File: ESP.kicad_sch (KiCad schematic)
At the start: 15 parts, among them J1 Conn_01x20_Pin, J2 Conn_01x20_Pin, J3 Conn_01x04_Pin, SW1 SW_Push, SW2 SW_Push, U3 AMS1117-3.3, U4 ESP32-S3-WROOM-1

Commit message: chore: add README (#2)
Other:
- title: (none) -> ESP32 PoE
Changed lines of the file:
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@@
 	(generator_version "9.0")
 	(paper "A4")
+	(title_block
+		(title "ESP32 PoE")
+		(rev "v0.1.0")
+	)
 	(rectangle
 		(start 16.51 161.29)

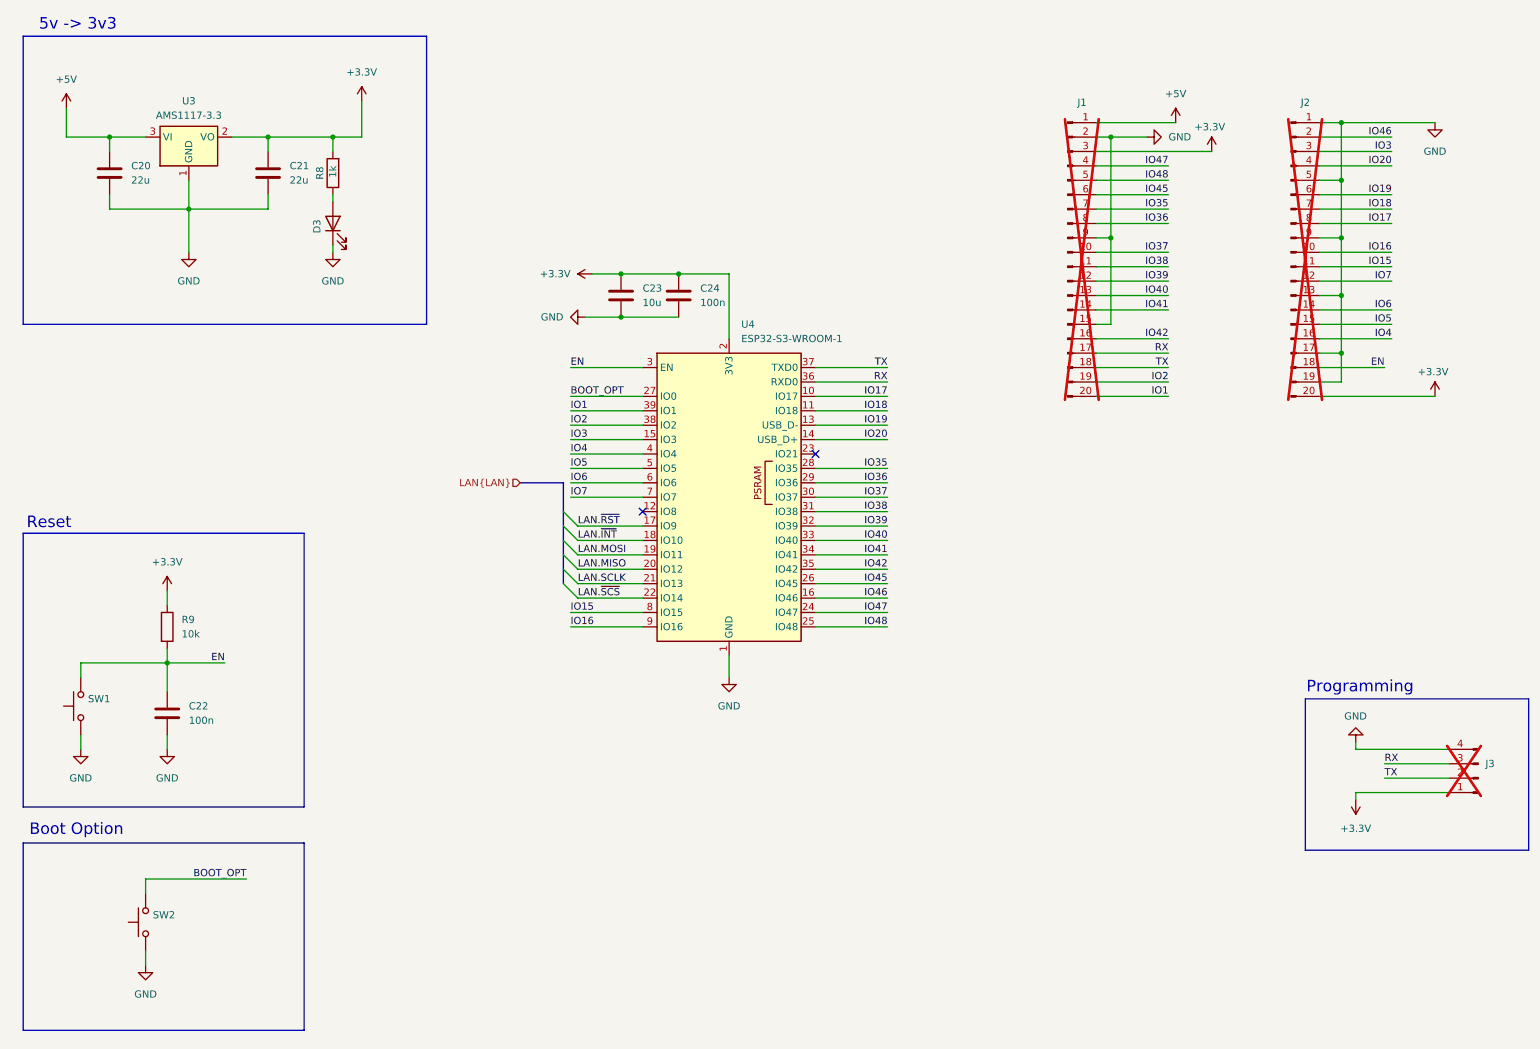
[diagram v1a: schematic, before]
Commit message: feat: redesign to smaller form factor
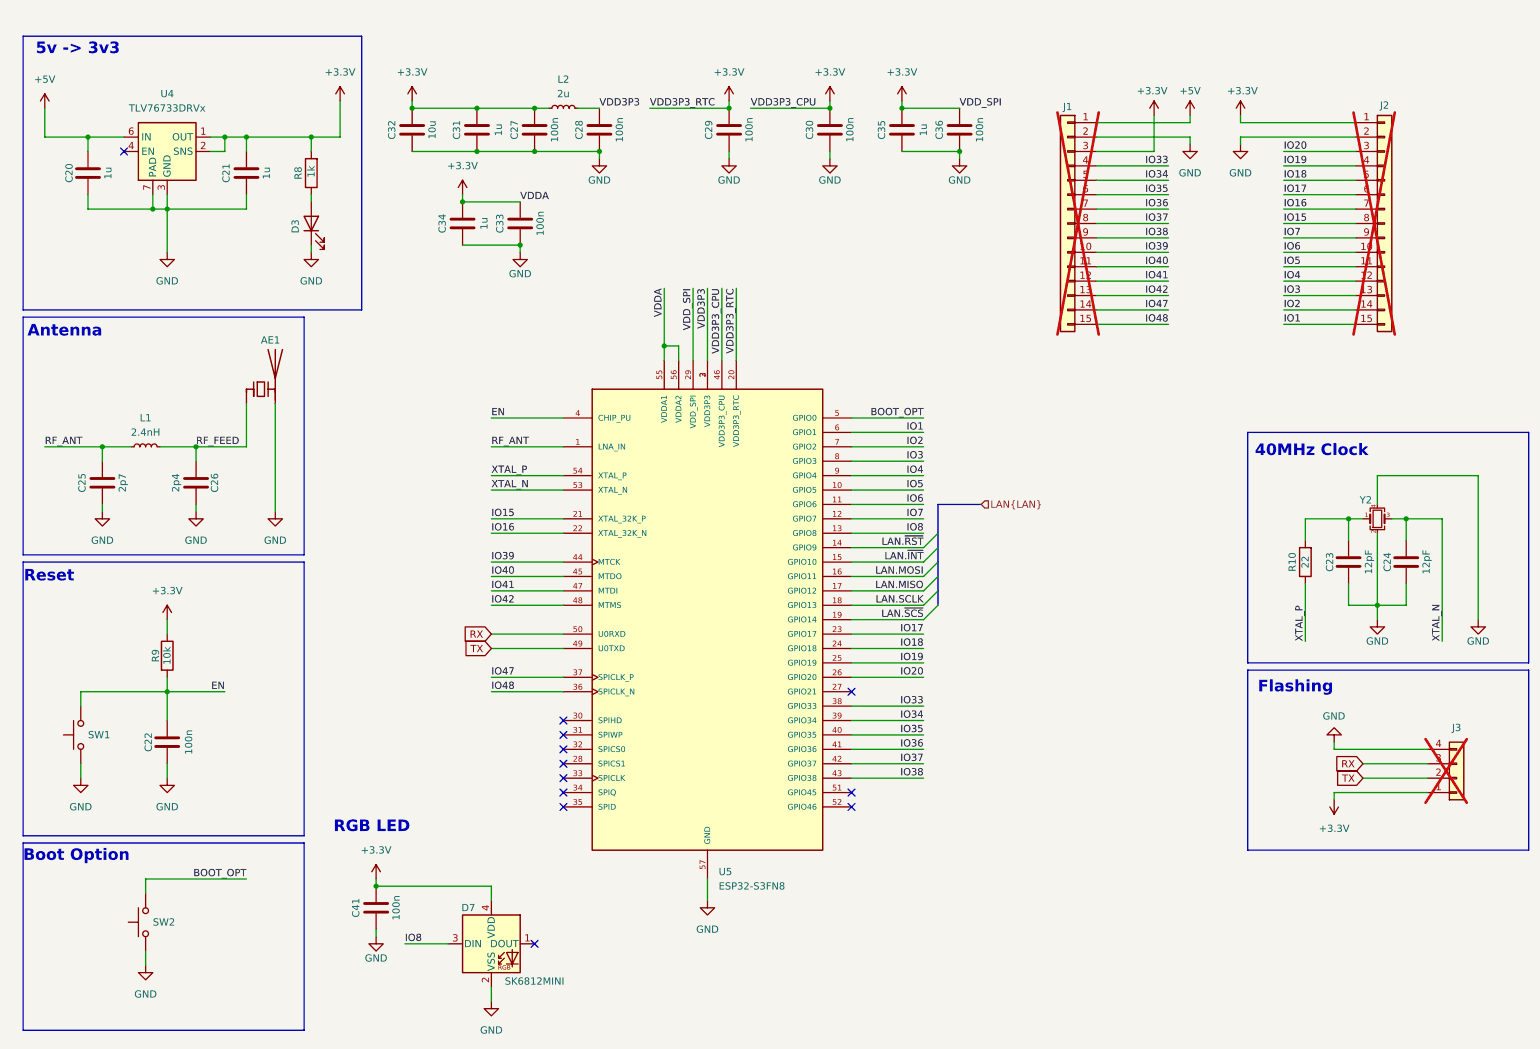
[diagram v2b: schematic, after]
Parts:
- removed C23: 10u, Capacitor_SMD:C_0603_1608Metric, symbol Device:C
- removed C24: 100n, Capacitor_SMD:C_0603_1608Metric, symbol Device:C
- removed U3: AMS1117-3.3, Package_TO_SOT_SMD:SOT-223-3_TabPin2, symbol Regulator_Linear:AMS1117-3.3
- removed U4: ESP32-S3-WROOM-1, RF_Module:ESP32-S3-WROOM-1, symbol RF_Module:ESP32-S3-WROOM-1
- added AE1: Ant_RFECA3216060A1T_1206, Hardware Components:Ant_RFECA3216060A1T, symbol Hardware Components:Ant_RFECA3216060A1T_1206
- added C23, C24: 12pF, Hardware Components:C_0402_1005Metric, symbol Hardware Components:C_12p_0402_50V
- added C25: 2p7, Hardware Components:C_0402_1005Metric, symbol Hardware Components:C_2p7_0402_50V
- added C26: 2p4, Hardware Components:C_0402_1005Metric, symbol Device:C
- added C27, C28, C29, C30, C33, C36, C41: 100n, Hardware Components:C_0402_1005Metric, symbol Hardware Components:C_100n_0402_16V
- added C31, C34, C35: 1u, Hardware Components:C_0402_1005Metric, symbol Hardware Components:C_1u_0402_10V
- added C32: 10u, Hardware Components:C_0402_1005Metric, symbol Hardware Components:C_10u_0402_10V
- added D7: SK6812MINI, Hardware Components:LED_SK6812MINI, symbol Hardware Components:LED_SK6812MINI
- added L1: 2.4nH, Hardware Components:L_0402_1005Metric, symbol Hardware Components:L_2n4_800mA_TDK_MLG1005S2N4BT000
- added L2: 2u, Hardware Components:L_0402_1005Metric, symbol Hardware Components:L_2u_900mA_TDK-MLG1005S2N0BT000
- added R10: 22, Hardware Components:R_0402_1005Metric, symbol Hardware Components:R_22_0402_50V
- added U4: TLV76733DRVx, Hardware Components:WSON-6-1EP_2x2mm_P0.65mm_EP1x1.6mm_ThermalVias, symbol Hardware Components:Conv_TLV76733DRVx
- added U5: ESP32-S3FN8, Hardware Components:MCU_ESP32-S3FN8, symbol Hardware Components:MCU_ESP32-S3FN8
- added Y2: ECS-400-10-37B2-CKM-TR, Hardware Components:Oscillator_ECS_400-10-37B2-CKM-TR, symbol Hardware Components:Oscillator_40MHz_ECS-400-10-37B2-CKM-TR
- C20, C21: value 22u -> 1u; footprint Capacitor_SMD:C_0603_1608Metric -> Hardware Components:C_0402_1005Metric; symbol Device:C -> Hardware Components:C_1u_0402_10V; JLCPCB Part # C59461 -> C14445; MPN CL10A226MQ8NRNC -> CL05A105KP5NNNC
- C22: footprint Capacitor_SMD:C_0603_1608Metric -> Hardware Components:C_0402_1005Metric; symbol Device:C -> Hardware Components:C_100n_0402_16V; JLCPCB Part # C1591 -> C1525; MPN CL10B104KB8NNNC -> CL05B104KO5NNNC
- D3: footprint LED_SMD:LED_0603_1608Metric -> Hardware Components:LED_0603_1608Metric; symbol HomeLabIO:LED -> Hardware Components:LED_R_0603_LTST-C191KRKT
- J1, J2: value Conn_01x20_Pin -> Conn_01x15_Pin; footprint Connector_PinHeader_2.54mm:PinHeader_1x20_P2.54mm_Vertical -> Connector_PinHeader_2.54mm:PinHeader_1x15_P2.54mm_Vertical; symbol Connector:Conn_01x20_Pin -> Connector_Generic:Conn_01x15
- J3: symbol Connector:Conn_01x04_Pin -> Connector_Generic:Conn_01x04
- R8: footprint Resistor_SMD:R_0402_1005Metric -> Hardware Components:R_0402_1005Metric; symbol HomeLabIO:R -> Hardware Components:R_1k_0402_75V
- R9: footprint Resistor_SMD:R_0603_1608Metric -> Hardware Components:R_0402_1005Metric; symbol Device:R -> Hardware Components:R_10k_0402_50V; JLCPCB Part # C2091877 -> C202396; MPN CR0603AFX-1002EAS -> CR0402-FX-1002GLF; Manufacturer BOURNS -> Bourns
- SW1, SW2: footprint ESP32PoE:SMD,3x4mm -> Hardware Components:SW_PTS815SJM250SMTRLFS; symbol Switch:SW_Push -> Hardware Components:SW_Push_4.2x3.2; JLCPCB Part # C455280 -> C139797; MPN TS-1088R-02026 -> SKRPACE010; Manufacturer XUNPU -> ALPSALPINE
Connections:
- net IO45 is gone; now on net IO35: J1.6 (Pin_6)
- net IO46 is gone; now on net GND: J2.2 (Pin_2)
- net +3.3V: now also J2.1 (Pin_1), C27.1, C29.1, C30.1, C31.1, C32.1, C33.1, C34.1, C35.1, C36.1, C41.1, D7.4 (VDD), L2.1, U4.1 (OUT), U4.2 (SNS), U5.20 (VDD3P3_RTC), U5.29 (VDD_SPI), U5.46 (VDD3P3_CPU), U5.55 (VDDA1), U5.56 (VDDA2); no longer J2.20 (Pin_20)
- net +5V: now also U4.6 (IN)
- net BOOT_OPT: now also U5.5 (GPIO0)
- net EN: now also U5.4 (CHIP_PU); no longer J2.18 (Pin_18)
- net GND: now also AE1.2 (PCB_Trace), C23.2, C24.2, C25.2, C26.1, C27.2, C28.2, C29.2, C30.2, C31.2, C32.2, C33.2, C34.2, C35.2, C36.2, C41.2, D7.2 (VSS), U4.3 (GND), U4.5 (GND), U4.7 (PAD), U5.57 (GND), Y2.2, Y2.4; no longer J1.15 (Pin_15), J1.9 (Pin_9), J2.1 (Pin_1), J2.13 (Pin_13), J2.17 (Pin_17), J2.19 (Pin_19), J2.5 (Pin_5), J2.9 (Pin_9)
- net IO1: now also J2.15 (Pin_15), U5.6 (GPIO1); no longer J1.20 (Pin_20)
- net IO15: now also J2.8 (Pin_8), U5.21 (XTAL_32K_P); no longer J2.11 (Pin_11)
- net IO16: now also J2.7 (Pin_7), U5.22 (XTAL_32K_N); no longer J2.10 (Pin_10)
- net IO17: now also J2.6 (Pin_6), U5.23 (GPIO17); no longer J2.8 (Pin_8)
- net IO18: now also J2.5 (Pin_5), U5.24 (GPIO18); no longer J2.7 (Pin_7)
- net IO19: now also J2.4 (Pin_4), U5.25 (GPIO19); no longer J2.6 (Pin_6)
- net IO2: now also J2.14 (Pin_14), U5.7 (GPIO2); no longer J1.19 (Pin_19)
- net IO20: now also J2.3 (Pin_3), U5.26 (GPIO20); no longer J2.4 (Pin_4)
- net IO3: now also J2.13 (Pin_13), U5.8 (GPIO3); no longer J2.3 (Pin_3)
- net IO35: now also U5.40 (GPIO35); no longer J1.7 (Pin_7)
- net IO36: now also J1.7 (Pin_7), U5.41 (GPIO36); no longer J1.8 (Pin_8)
- net IO37: now also J1.8 (Pin_8), U5.42 (GPIO37); no longer J1.10 (Pin_10)
- net IO38: now also J1.9 (Pin_9), U5.43 (GPIO38); no longer J1.11 (Pin_11)
- net IO39: now also J1.10 (Pin_10), U5.44 (MTCK); no longer J1.12 (Pin_12)
- net IO4: now also J2.12 (Pin_12), U5.9 (GPIO4); no longer J2.16 (Pin_16)
- net IO40: now also J1.11 (Pin_11), U5.45 (MTDO); no longer J1.13 (Pin_13)
- net IO41: now also J1.12 (Pin_12), U5.47 (MTDI); no longer J1.14 (Pin_14)
- net IO42: now also J1.13 (Pin_13), U5.48 (MTMS); no longer J1.16 (Pin_16)
- net IO47: now also J1.14 (Pin_14), U5.37 (SPICLK_P); no longer J1.4 (Pin_4)
- net IO48: now also J1.15 (Pin_15), U5.36 (SPICLK_N); no longer J1.5 (Pin_5)
- net IO5: now also J2.11 (Pin_11), U5.10 (GPIO5); no longer J2.15 (Pin_15)
- net IO6: now also J2.10 (Pin_10), U5.11 (GPIO6); no longer J2.14 (Pin_14)
- net IO7: now also J2.9 (Pin_9), U5.12 (GPIO7); no longer J2.12 (Pin_12)
- net LAN.MISO: now also U5.17 (GPIO12)
- net LAN.MOSI: now also U5.16 (GPIO11)
- net LAN.SCLK: now also U5.18 (GPIO13)
- net LAN.~{INT}: now also U5.15 (GPIO10)
- net LAN.~{RST}: now also U5.14 (GPIO9)
- net LAN.~{SCS}: now also U5.19 (GPIO14)
- net RX: now also U5.50 (U0RXD); no longer J1.17 (Pin_17)
- net TX: now also U5.49 (U0TXD); no longer J1.18 (Pin_18)
- new net: C23.1, R10.2, Y2.1
- new net IO33: J1.4 (Pin_4), U5.38 (GPIO33)
- new net IO34: J1.5 (Pin_5), U5.39 (GPIO34)
- new net IO8: D7.3 (DIN), U5.13 (GPIO8)
- new net RF_ANT: C25.1, L1.1, U5.1 (LNA_IN)
- new net RF_FEED: AE1.1 (FEED), C26.2, L1.2
- new net VDD3P3: C28.1, L2.2, U5.2 (VDD3P3), U5.3 (VDD3P3)
- new net XTAL_N: C24.1, U5.53 (XTAL_N), Y2.3
- new net XTAL_P: R10.1, U5.54 (XTAL_P)
- no-connect marks 2 -> 12
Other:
- note added: "40MHz Clock"
- note added: "Antenna"
- note added: "Flashing"
- note added: "RGB LED"
- note removed: "Programming"
- moved on the sheet: C20, C21, C22, D3, R8, R9, SW1
